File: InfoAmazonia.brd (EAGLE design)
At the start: 95.2 x 70.4 mm, 80 parts, among them IC1 LM2662, IC2 ADAFRUIT FONA, IC3 MIC29302AWD, IC4 4050D, IC5 TL032C, IC6 CA3140AM Z, IC7 TL081BCDG4, IC8 SHT20, IC9 NE555, J1 BNCPTH, J2 BNCPTH, J3 BNCPTH, U1 ARDUINO-MEGAPRO, U2 MPL3115A2, U3 USD-SOCKETNEW, U4 ALS-PT19

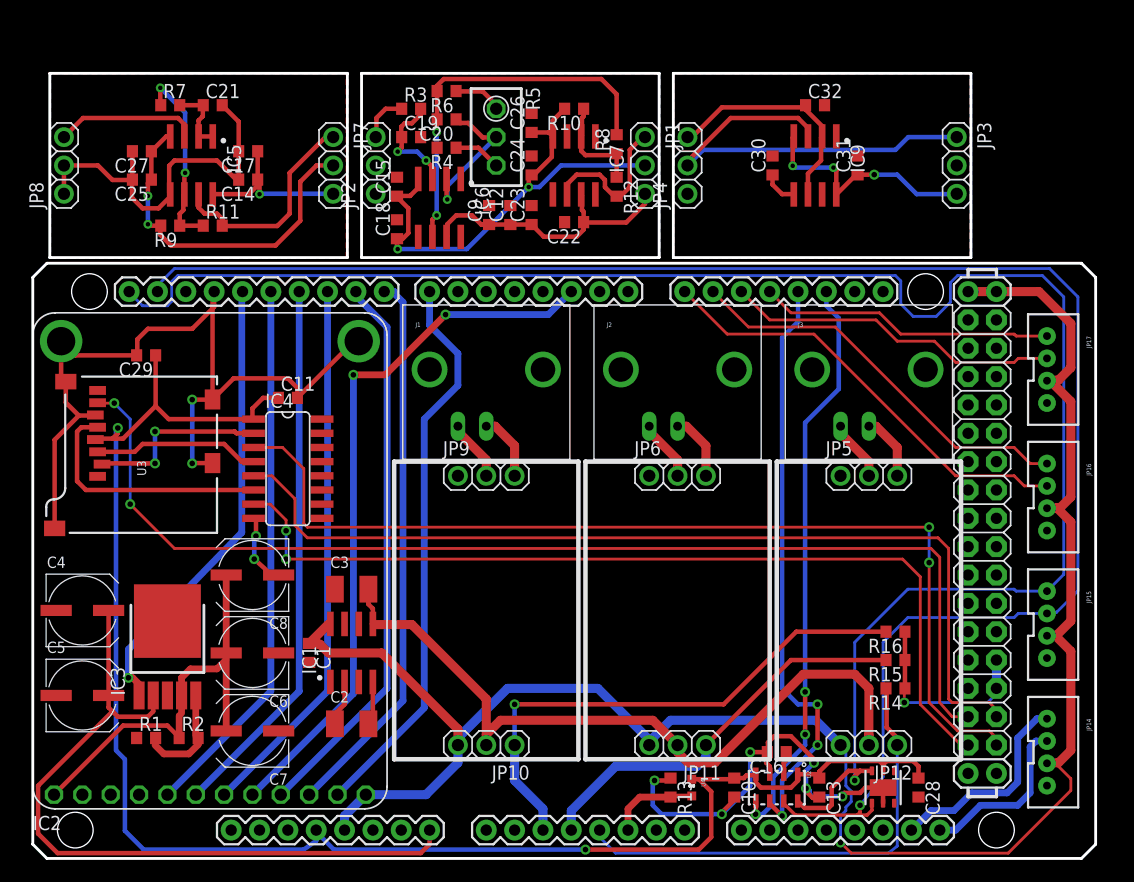
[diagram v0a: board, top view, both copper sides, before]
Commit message: - Mudanças cosmeticas na parte dos sensores
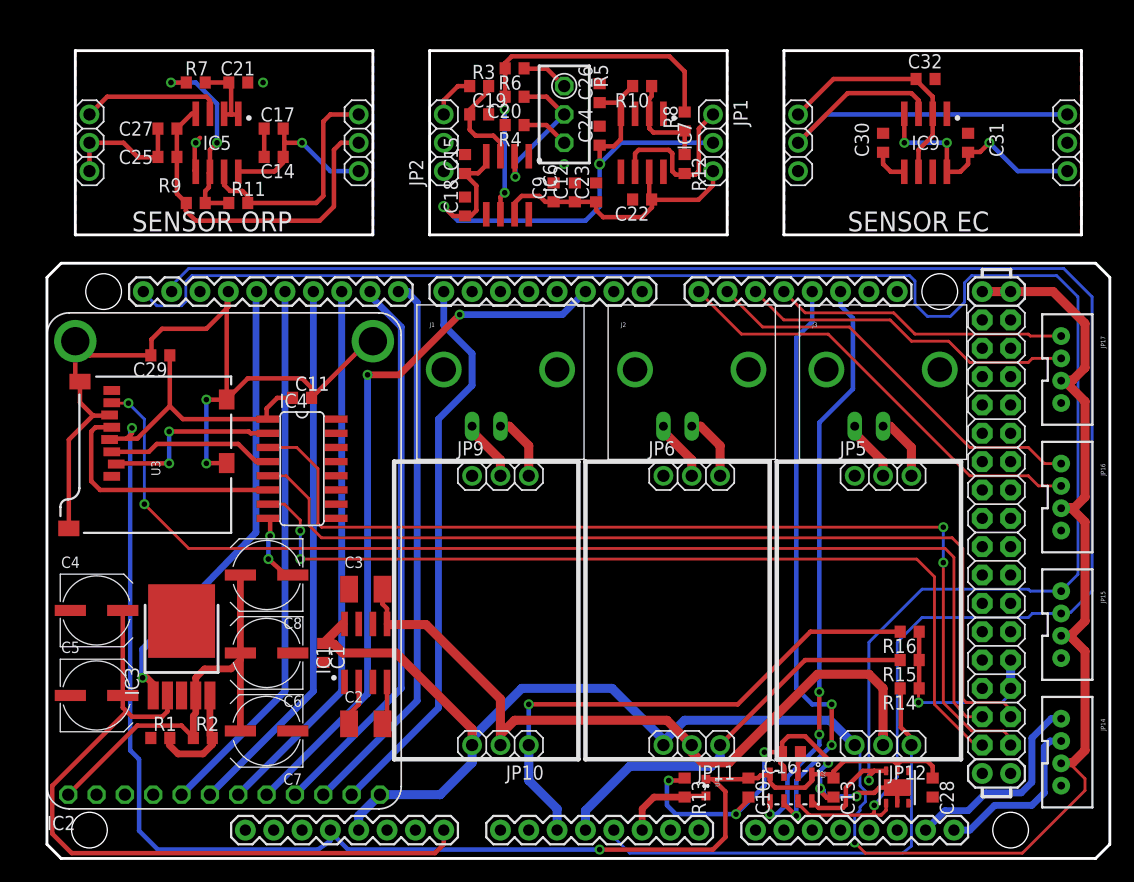
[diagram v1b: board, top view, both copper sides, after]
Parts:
- moved C32 10.2 mm to (78.7, 69.8)
- moved C30 10.1 mm to (74.9, 64.1)
- moved JP4 10.1 mm to (67.3, 64.1)
- moved C31 10.1 mm to (82.5, 64.1)
- moved IC9 10.1 mm to (78.7, 64.1)
- moved JP3 10.1 mm to (91.4, 64.1)
- moved C26 6.65 mm to (49.5, 68.6)
- moved C24 6.65 mm to (49.5, 64.8)
- moved C18 6.43 mm to (37.5, 58.4)
- moved IC7 6.43 mm to (53.3, 64.1)
- moved JP2 6.43 mm to (35.6, 64.1)
- moved C15 6.43 mm to (37.5, 62.2)
- moved C22 6.43 mm to (53.3, 59.1)
- moved R10 6.43 mm to (53.3, 69.2)
- moved R8 6.43 mm to (57.1, 66.0)
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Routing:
- net GND: track 158.3 -> 141.5 mm, vias 10 -> 13
- net -5V: track 144.5 -> 150.7 mm, vias 4 -> 2
- net ORP_SENSOR: track 19.7 -> 21.5 mm
- net +5V: track 234.5 -> 236.1 mm
- net PH_SENSOR: track 13.6 -> 15.2 mm
- net N$2: track 9.86 -> 9.07 mm, vias 2 -> 0
- net N$17: track 17.2 -> 17.8 mm
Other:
- board size 95.2 x 70.4 mm -> 95.2 x 72.4 mm
- board text added: "SENSOR EC"
- board text added: "SENSOR ORP"

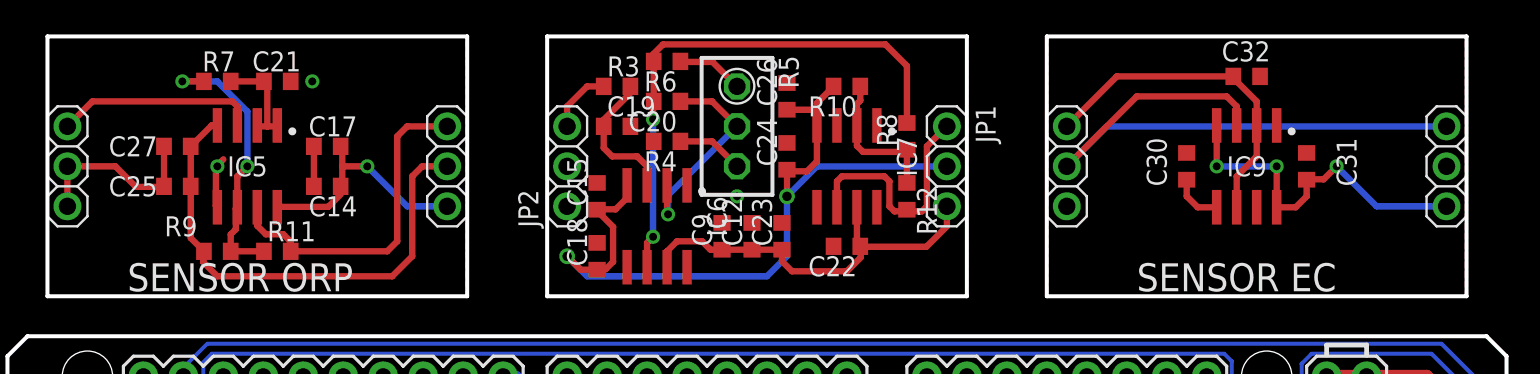
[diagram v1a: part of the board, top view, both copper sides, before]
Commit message: - Mudancas no silkscreen da placa
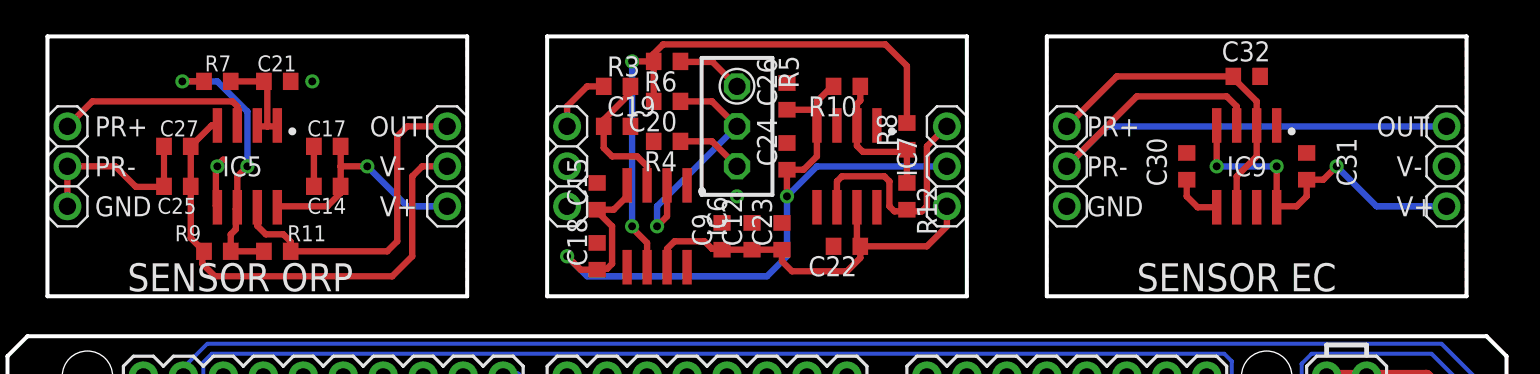
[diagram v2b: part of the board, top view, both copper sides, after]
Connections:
- new net +VEC: C31.1, IC9.4, IC9.8, JP3.3
- new net +VORP: C14.1, C17.1, IC5.8, JP7.3
- new net +VPH: C12.1, C22.1, C23.1, C9.1, IC6.7, IC7.7, JP1.3
- new net -VORP: C25.1, C27.1, IC5.4, JP7.2, R9.2
- new net -VPH: C15.1, C18.1, C24.1, C26.1, IC6.4, IC7.4, JP1.2, R10.2
- net +5V: no longer C12.1, C14.1, C17.1, C22.1, C23.1, C31.1, C9.1, IC5.8, IC6.7, IC7.7, IC9.4, IC9.8, JP1.3, JP3.3, JP7.3
- net -5V: no longer C15.1, C18.1, C24.1, C25.1, C26.1, C27.1, IC5.4, IC6.4, IC7.4, JP1.2, JP3.2, JP7.2, R10.2, R9.2
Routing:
- net -5V: track 150.7 -> 67.9 mm, vias 2 -> 0
- net +5V: track 236.1 -> 172.8 mm, vias 5 -> 1
- net -VPH: track 0.00 -> 50.8 mm, vias 0 -> 2
- net -VORP: track 0.00 -> 31.8 mm
- net +VPH: track 0.00 -> 25.8 mm
- net +VEC: track 0.00 -> 22.6 mm, vias 0 -> 3
- net +VORP: track 0.00 -> 15.2 mm, vias 0 -> 1
- net N$4: track 34.8 -> 39.0 mm
- net N$3: track 13.5 -> 15.6 mm
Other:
- board text added: "GND"
- board text added: "OUT"
- board text added: "PR+"
- board text added: "PR-"
- board text added: "V+"
- board text added: "V-"

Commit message: - Ajustes depois do prototipo
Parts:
- C32: value 1uF -> 100nF
- moved J1 1.27 mm to (40.6, 37.5)
- moved J2 1.27 mm to (57.8, 37.5)
- moved J3 1.27 mm to (74.9, 37.5)
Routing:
- net +VBAT: track 39.0 -> 44.0 mm
- net N$1: track 5.96 -> 4.23 mm
- net N$9: track 5.50 -> 4.23 mm
- net N$13: track 5.87 -> 6.65 mm
- net N$11: track 5.96 -> 6.67 mm
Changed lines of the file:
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@@
 <setting verticaltext="up"/>
 </settings>
-<grid distance="0.025" unitdist="inch" unit="mm" style="lines" multiple="1" display="yes" altdistance="0.00625" altunitdist="inch" altunit="inch"/>
+<grid distance="0.025" unitdist="inch" unit="inch" style="lines" multiple="1" display="yes" altdistance="0.00625" altunitdist="inch" altunit="inch"/>
 <layers>
 <layer number="1" name="Top" color="4" fill="1" visible="yes" active="yes"/>
@@
 <layer number="49" name="Reference" color="14" fill="1" visible="no" active="yes"/>
 <layer number="50" name="dxf" color="7" fill="1" visible="no" active="no"/>
-<layer number="51" name="tDocu" color="7" fill="1" visible="no" active="yes"/>
+<layer number="51" name="tDocu" color="7" fill="1" visible="yes" active="yes"/>
 <layer number="52" name="bDocu" color="7" fill="1" visible="no" active="yes"/>
 <layer number="53" name="tGND_GNDA" color="7" fill="9" visible="no" active="no"/>
@@
 </element>
 <element name="IC8" library="InfoAmazonia" package="SHT2X" value="SHT20" x="76.2" y="6.35" smashed="yes"/>
-<element name="J2" library="InfoAmazonia" package="BNC" value="BNCPTH" x="57.785" y="38.735" smashed="yes">
-<attribute name="NAME" x="51.435" y="47.625" size="0.4064" layer="25" font="vector" ratio="15"/>
-<attribute name="VALUE" x="51.435" y="46.355" size="0.4064" layer="27" font="vector" ratio="15" rot="SR0"/>
-</element>
-<element name="J1" library="InfoAmazonia" package="BNC" value="BNCPTH" x="40.64" y="38.735" smashed="yes">
-<attribute name="NAME" x="34.29" y="47.625" size="0.4064" layer="25" font="vector" ratio="15"/>
-<attribute name="VALUE" x="34.29" y="46.355" size="0.4064" layer="27" font="vector" ratio="15" rot="SR0"/>
+<element name="J2" library="InfoAmazonia" package="BNC" value="BNCPTH" x="57.785" y="37.465" smashed="yes">
+<attribute name="NAME" x="51.435" y="46.355" size="0.4064" layer="25" font="vector" ratio="15"/>
+<attribute name="VALUE" x="51.435" y="45.085" size="0.4064" layer="27" font="vector" ratio="15" rot="SR0"/>
+</element>
+<element name="J1" library="InfoAmazonia" package="BNC" value="BNCPTH" x="40.64" y="37.465" smashed="yes">
+<attribute name="NAME" x="34.29" y="46.355" size="0.4064" layer="25" font="vector" ratio="15"/>
+<attribute name="VALUE" x="34.29" y="45.085" size="0.4064" layer="27" font="vector" ratio="15" rot="SR0"/>
 </element>
 <element name="R3" library="InfoAmazonia" package="R0603" value="4M7" x="38.735" y="69.215" smashed="yes">
@@
 <attribute name="VALUE" x="55.245" y="6.985" size="1.27" layer="27" font="vector" ratio="15" rot="R270"/>
 </element>
-<element name="J3" library="InfoAmazonia" package="BNC" value="BNCPTH" x="74.93" y="38.735" smashed="yes">
-<attribute name="NAME" x="68.58" y="47.625" size="0.4064" layer="25" font="vector" ratio="15"/>
-<attribute name="VALUE" x="68.58" y="46.355" size="0.4064" layer="27" font="vector" ratio="15" rot="SR0"/>
+<element name="J3" library="InfoAmazonia" package="BNC" value="BNCPTH" x="74.93" y="37.465" smashed="yes">
+<attribute name="NAME" x="68.58" y="46.355" size="0.4064" layer="25" font="vector" ratio="15"/>
+<attribute name="VALUE" x="68.58" y="45.085" size="0.4064" layer="27" font="vector" ratio="15" rot="SR0"/>
 </element>
 <element name="C29" library="InfoAmazonia" package="C0603" value="10uF" x="10.16" y="45.085" smashed="yes" rot="R180">
@@
 <attribute name="VALUE" x="87.63" y="61.595" size="1.27" layer="27" font="vector" ratio="15" rot="R90"/>
 </element>
-<element name="C32" library="InfoAmazonia" package="C0603" value="1uF" x="78.74" y="69.85" smashed="yes">
+<element name="C32" library="InfoAmazonia" package="C0603" value="100nF" x="78.74" y="69.85" smashed="yes">
 <attribute name="NAME" x="77.1525" y="70.8025" size="1.27" layer="25" font="vector" ratio="15"/>
 <attribute name="VALUE" x="80.645" y="69.85" size="1.27" layer="27" font="vector" ratio="15"/>
@@
 <wire x1="17.335" y1="11.43" x2="17.335" y2="18.415" width="0.6096" layer="1"/>
 <wire x1="13.12" y1="10.795" x2="13.12" y2="10.85125" width="0.4064" layer="1"/>
-<wire x1="13.12" y1="10.85125" x2="12.065" y2="11.90625" width="0.4064" layer="1"/>
-<wire x1="12.065" y1="11.90625" x2="8.09625" y2="11.90625" width="0.4064" layer="1"/>
-<wire x1="8.09625" y1="11.90625" x2="1.905" y2="5.715" width="0.4064" layer="1"/>
 <wire x1="17.335" y1="18.415" x2="17.335" y2="25.4" width="0.6096" layer="1"/>
+<wire x1="1.905" y1="5.715" x2="1.905" y2="6.35" width="0.4064" layer="1"/>
+<wire x1="1.905" y1="6.35" x2="3.81" y2="8.255" width="0.4064" layer="1"/>
+<wire x1="3.81" y1="8.255" x2="15.875" y2="8.255" width="0.4064" layer="1"/>
+<wire x1="17.335" y1="11.43" x2="17.335" y2="9.715" width="0.4064" layer="1"/>
+<wire x1="17.335" y1="9.715" x2="15.875" y2="8.255" width="0.4064" layer="1"/>
 </signal>
 <signal name="N$18">
@@
 <contactref element="J1" pad="S"/>
 <contactref element="JP9" pad="3"/>
-<wire x1="40.64" y1="38.735" x2="41.43375" y2="38.735" width="0.8128" layer="1"/>
-<wire x1="41.43375" y1="38.735" x2="43.18" y2="36.98875" width="0.8128" layer="1"/>
-<wire x1="43.18" y1="36.98875" x2="43.18" y2="34.29" width="0.8128" layer="1"/>
+<wire x1="43.18" y1="34.29" x2="40.64" y2="36.83" width="0.8128" layer="1"/>
+<wire x1="40.64" y1="36.83" x2="40.64" y2="37.465" width="0.8128" layer="1"/>
 </signal>
 <signal name="N$9">
 <contactref element="JP9" pad="2"/>
 <contactref element="J1" pad="GND"/>
-<wire x1="38.1" y1="38.735" x2="38.1" y2="38.25875" width="0.8128" layer="1"/>
-<wire x1="38.1" y1="38.25875" x2="40.64" y2="35.71875" width="0.8128" layer="1"/>
-<wire x1="40.64" y1="35.71875" x2="40.64" y2="34.29" width="0.8128" layer="1"/>
+<wire x1="40.64" y1="34.29" x2="38.1" y2="36.83" width="0.8128" layer="1"/>
+<wire x1="38.1" y1="36.83" x2="38.1" y2="37.465" width="0.8128" layer="1"/>
 </signal>
 <signal name="N$11">
 <contactref element="JP6" pad="3"/>
 <contactref element="J2" pad="S"/>
-<wire x1="57.785" y1="38.735" x2="58.57875" y2="38.735" width="0.8128" layer="1"/>
+<wire x1="57.785" y1="37.465" x2="58.57875" y2="38.735" width="0.8128" layer="1"/>
 <wire x1="58.57875" y1="38.735" x2="60.325" y2="36.98875" width="0.8128" layer="1"/>
 <wire x1="60.325" y1="36.98875" x2="60.325" y2="34.29" width="0.8128" layer="1"/>
@@
 <contactref element="JP6" pad="2"/>
 <contactref element="J2" pad="GND"/>
-<wire x1="55.245" y1="38.735" x2="55.245" y2="38.25875" width="0.8128" layer="1"/>
+<wire x1="55.245" y1="37.465" x2="55.245" y2="38.25875" width="0.8128" layer="1"/>
 <wire x1="55.245" y1="38.25875" x2="57.785" y2="35.71875" width="0.8128" layer="1"/>
 <wire x1="57.785" y1="35.71875" x2="57.785" y2="34.29" width="0.8128" layer="1"/>
@@
 <contactref element="JP5" pad="3"/>
 <contactref element="J3" pad="S"/>
-<wire x1="74.93" y1="38.735" x2="75.565" y2="38.735" width="0.8128" layer="1"/>
+<wire x1="74.93" y1="37.465" x2="75.565" y2="38.735" width="0.8128" layer="1"/>
 <wire x1="75.565" y1="38.735" x2="77.47" y2="36.83" width="0.8128" layer="1"/>
 <wire x1="77.47" y1="36.83" x2="77.47" y2="34.29" width="0.8128" layer="1"/>
@@
 <contactref element="JP5" pad="2"/>
 <contactref element="J3" pad="GND"/>
-<wire x1="72.39" y1="38.735" x2="72.39" y2="38.1" width="0.8128" layer="1"/>
+<wire x1="72.39" y1="37.465" x2="72.39" y2="38.1" width="0.8128" layer="1"/>
 <wire x1="72.39" y1="38.1" x2="74.93" y2="35.56" width="0.8128" layer="1"/>
 <wire x1="74.93" y1="35.56" x2="74.93" y2="34.29" width="0.8128" layer="1"/>

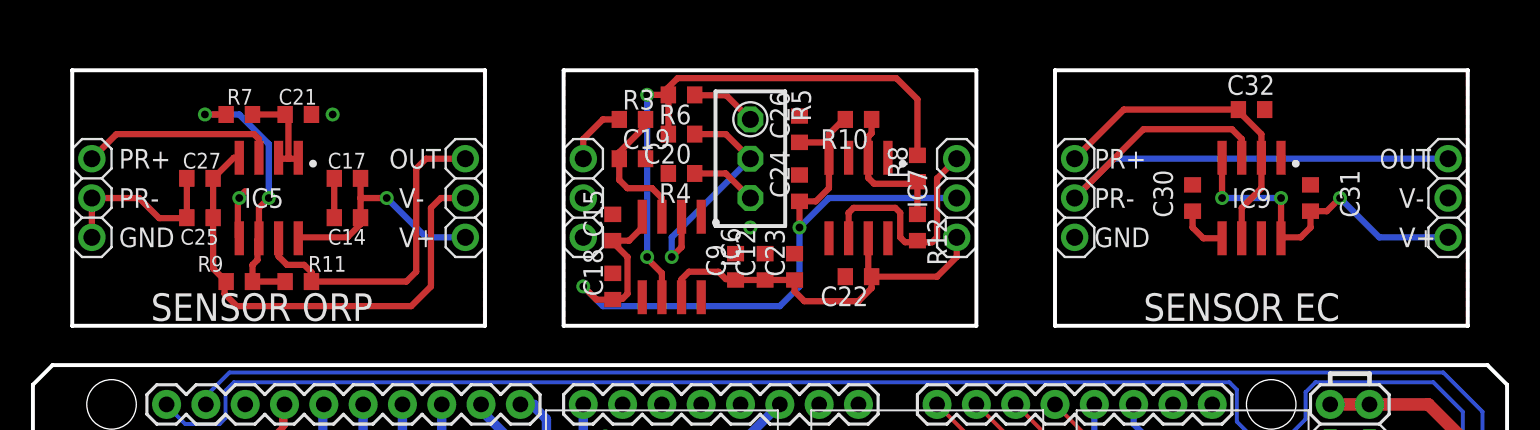
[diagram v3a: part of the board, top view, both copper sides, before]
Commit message: - Alteracao nos modulos externos. Agora devem caber em uma protoboard.
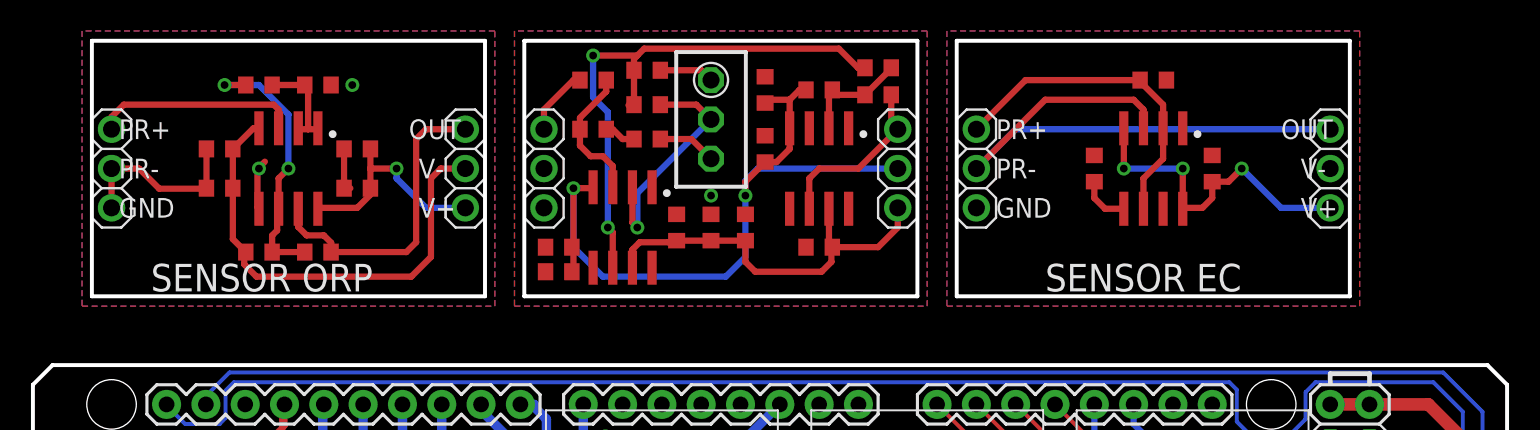
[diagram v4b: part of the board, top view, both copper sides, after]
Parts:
- moved R12 8.94 mm to (54.6, 70.8), turned to 0 degrees
- moved JP3 7.85 mm to (83.8, 66.0)
- moved R8 6.99 mm to (54.6, 72.5), turned to 180 degrees
- moved C30 6.63 mm to (68.6, 66.0)
- moved JP4 6.63 mm to (61.0, 66.0)
- moved C31 6.63 mm to (76.2, 66.0)
- moved C32 6.63 mm to (72.4, 71.8)
- moved IC9 6.63 mm to (72.4, 66.0)
- moved C9 4.58 mm to (41.6, 62.2)
- moved C12 4.32 mm to (43.8, 62.2)
- moved JP1 4.26 mm to (55.9, 66.0)
- moved C23 4.07 mm to (46.0, 62.2)
- moved C15 3.72 mm to (34.0, 61.0), turned to 180 degrees
- moved IC6 3.70 mm to (38.1, 62.2)
- moved C18 3.62 mm to (34.0, 59.4), turned to 180 degrees
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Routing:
- net PH_SENSOR: track 15.2 -> 11.4 mm
- net N$4: track 39.0 -> 36.1 mm
- net N$5: track 9.51 -> 7.26 mm
- net GND: track 141.5 -> 143.5 mm
- net -VPH: track 50.8 -> 49.0 mm
- net +VEC: track 22.6 -> 21.3 mm
- net EC_SENSOR: track 39.3 -> 38.0 mm
- net ORP_SENSOR: track 21.5 -> 20.2 mm
- net -VORP: track 31.8 -> 30.6 mm
- net +VORP: track 15.2 -> 14.3 mm
- net N$8: track 4.25 -> 3.54 mm
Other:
- board size 95.2 x 72.4 mm -> 95.2 x 74.3 mm
